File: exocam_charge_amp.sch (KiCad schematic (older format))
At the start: 17 parts, among them J1 jstsh6x1, U1 TLV2771CDBVT, U2 TLV2771CDBVT

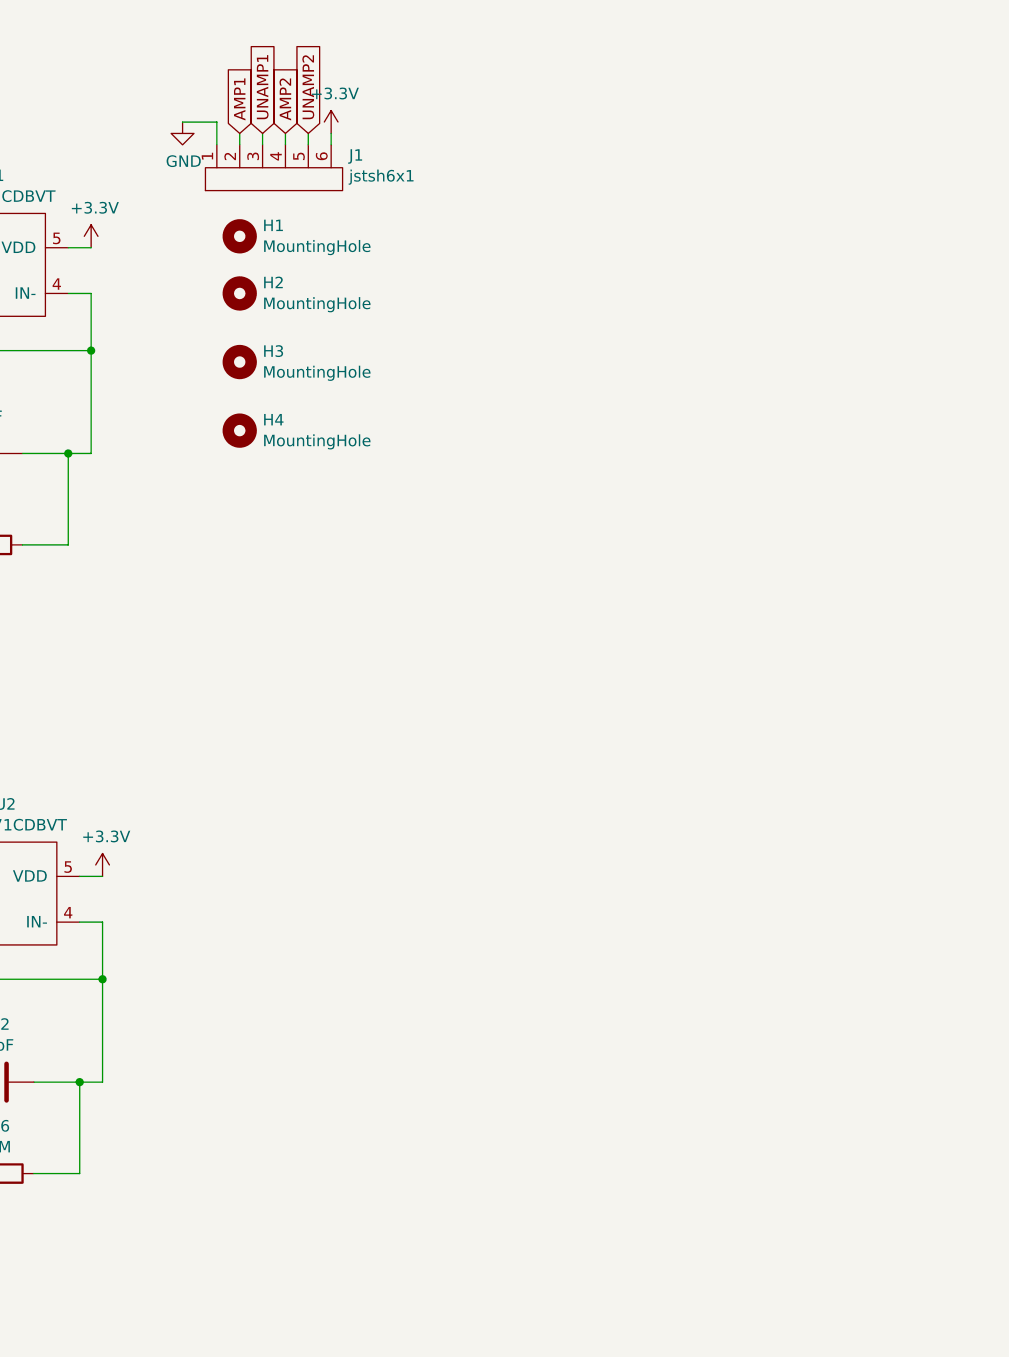
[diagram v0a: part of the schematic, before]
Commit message: updated shoulder to include the 3 amps
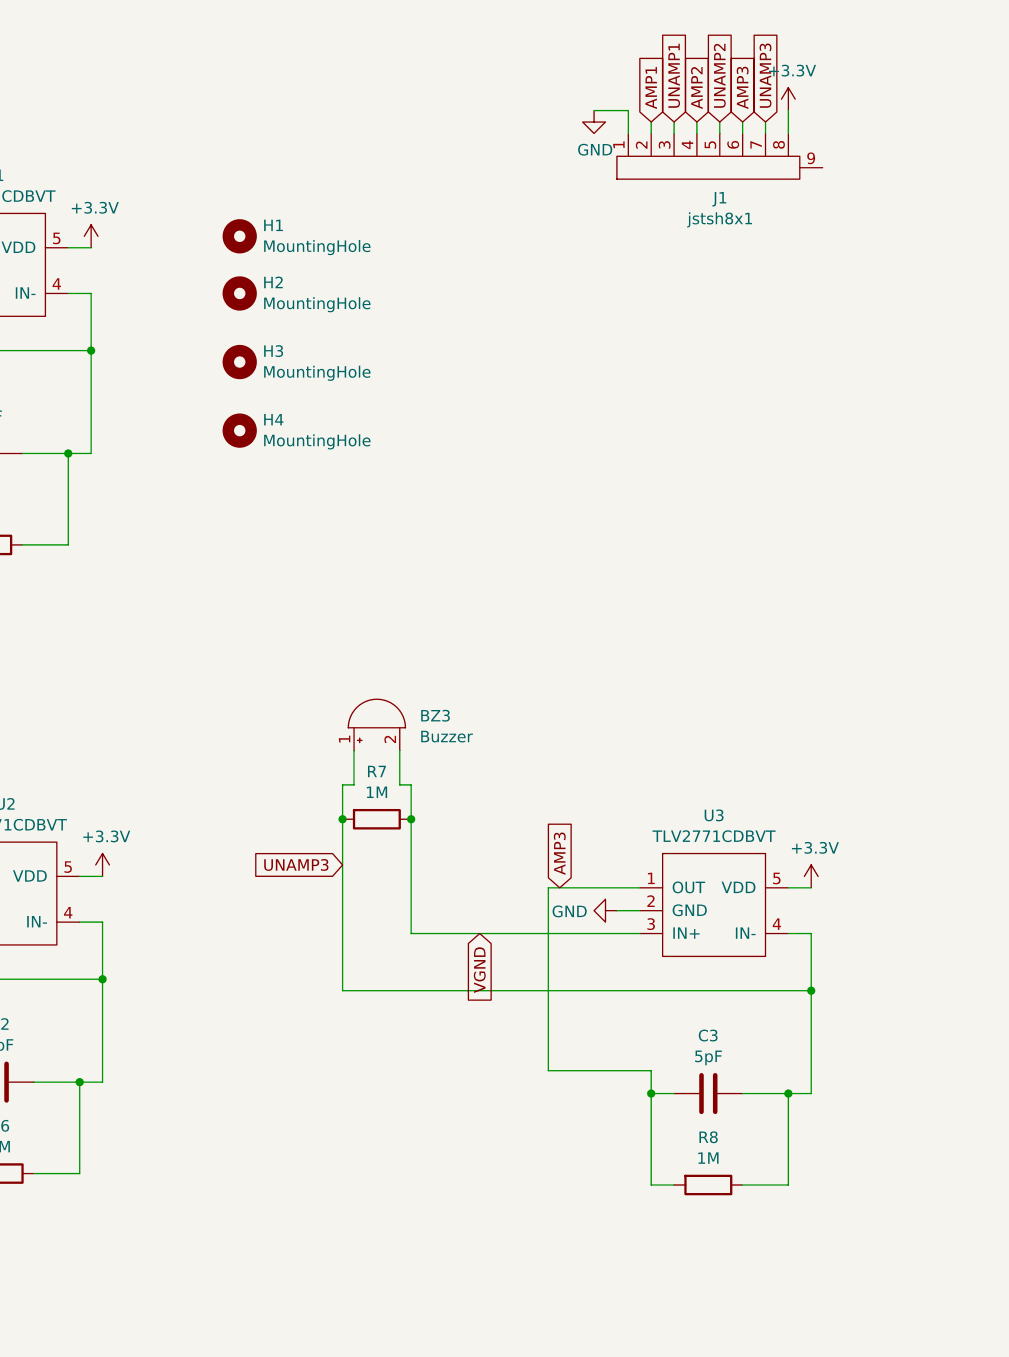
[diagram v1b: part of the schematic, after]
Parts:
- removed J1: jstsh6x1, exocam_charge_amp:jstsh6x1, symbol exocam_charge_amp:jstsh6x1
- added BZ3: Buzzer, exocam_charge_amp:jstsh2x1, symbol Device:Buzzer
- added C3: 5pF, exocam_charge_amp:0603_R, symbol Device:C
- added J1: jstsh8x1, exocam_charge_amp:jstsh8x1, symbol exocam_charge_amp:jstsh8x1
- added R7, R8: 1M, exocam_charge_amp:0603_R, symbol Device:R
- added U3: TLV2771CDBVT, exocam_charge_amp:TLV2271DBV, symbol exocam_charge_amp:TLV2771CDBVT
- BZ1: footprint exocam_charge_amp:piezo_buzzer -> exocam_charge_amp:piezo_buzzer_alt
- BZ2: footprint exocam_charge_amp:piezo_buzzer_alt -> exocam_charge_amp:jstsh2x1
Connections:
- net +3V3: now also J1.8, U3.5 (VDD)
- net AMP1: now also J1.2
- net AMP2: now also J1.4
- net GND: now also J1.1, U3.2 (GND)
- net UNAMP1: now also J1.3
- net UNAMP2: now also J1.5
- net VGND: now also BZ3.2 (+), R7.1, U3.3 (IN+)
- new net AMP3: C3.2, J1.6, R8.2, U3.1 (OUT)
- new net UNAMP3: BZ3.1 (-), C3.1, J1.7, R7.2, R8.1, U3.4 (IN-)
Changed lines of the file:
@@
 F 0 "BZ1" V 1901 613 50  0000 R CNN
 F 1 "Buzzer" V 1810 613 50  0000 R CNN
-F 2 "exocam_charge_amp:piezo_buzzer" V 1825 900 50  0001 C CNN
+F 2 "exocam_charge_amp:piezo_buzzer_alt" V 1825 900 50  0001 C CNN
 F 3 "~" V 1825 900 50  0001 C CNN
 	1    1850 800
@@
 F 0 "BZ2" V 1951 3363 50  0000 R CNN
 F 1 "Buzzer" V 1860 3363 50  0000 R CNN
-F 2 "exocam_charge_amp:piezo_buzzer_alt" V 1875 3650 50  0001 C CNN
+F 2 "exocam_charge_amp:jstsh2x1" V 1875 3650 50  0001 C CNN
 F 3 "~" V 1875 3650 50  0001 C CNN
 	1    1900 3550
@@
 Text GLabel 2350 4450 3    50   Input ~ 0
 VGND
-$Comp
-L exocam_charge_amp:jstsh6x1 J1
-U 1 1 60E1AF6A
-P 4250 1150
-F 0 "J1" V 4304 522 50  0000 R CNN
-F 1 "jstsh6x1" V 4213 522 50  0000 R CNN
-F 2 "exocam_charge_amp:jstsh6x1" H 4200 1300 50  0001 C CNN
-F 3 "" H 4200 1300 50  0001 C CNN
-	1    4250 1150
-	0    -1   -1   0
-$EndComp
-$Comp
-L power:+3.3V #PWR0104
-U 1 1 60E1C732
-P 4800 1000
-F 0 "#PWR0104" H 4800 850 50  0001 C CNN
-F 1 "+3.3V" H 4815 1173 50  0000 C CNN
-F 2 "" H 4800 1000 50  0001 C CNN
-F 3 "" H 4800 1000 50  0001 C CNN
-	1    4800 1000
-	1    0    0    -1
-$EndComp
-Wire Wire Line
-	4800 1050 4800 1000
-$Comp
-L power:GND #PWR0105
-U 1 1 60E1EDAD
-P 4150 950
-F 0 "#PWR0105" H 4150 700 50  0001 C CNN
-F 1 "GND" H 4155 777 50  0000 C CNN
-F 2 "" H 4150 950 50  0001 C CNN
-F 3 "" H 4150 950 50  0001 C CNN
-	1    4150 950
-	1    0    0    -1
-$EndComp
-Wire Wire Line
-	4300 1050 4300 950
-Wire Wire Line
-	4300 950  4150 950
-Text GLabel 4400 1000 1    50   Input ~ 0
-AMP1
-Wire Wire Line
-	4400 1050 4400 1000
-Text GLabel 4500 1000 1    50   Input ~ 0
-UNAMP1
-Wire Wire Line
-	4500 1000 4500 1050
-Text GLabel 4600 1000 1    50   Input ~ 0
-AMP2
-Wire Wire Line
-	4600 1000 4600 1050
-Text GLabel 4700 1000 1    50   Input ~ 0
-UNAMP2
-Wire Wire Line
-	4700 1000 4700 1050
 Wire Wire Line
 	1750 3950 1750 4700
@@
 Text GLabel 2700 1500 1    50   Input ~ 0
 AMP1
+$Comp
+L Device:C C3
+U 1 1 60E53BF7
+P 6450 5200
+F 0 "C3" V 6198 5200 50  0000 C CNN
+F 1 "5pF" V 6289 5200 50  0000 C CNN
+F 2 "exocam_charge_amp:0603_R" H 6488 5050 50  0001 C CNN
+F 3 "~" H 6450 5200 50  0001 C CNN
+	1    6450 5200
+	0    1    1    0
+$EndComp
+Wire Wire Line
+	6200 5200 6300 5200
+Wire Wire Line
+	6600 5200 6800 5200
+$Comp
+L Device:R R8
+U 1 1 60E53BFF
+P 6450 5600
+F 0 "R8" V 6243 5600 50  0000 C CNN
+F 1 "1M" V 6334 5600 50  0000 C CNN
+F 2 "exocam_charge_amp:0603_R" V 6380 5600 50  0001 C CNN
+F 3 "~" H 6450 5600 50  0001 C CNN
+	1    6450 5600
+	0    1    1    0
+$EndComp
+Wire Wire Line
+	6300 5600 6200 5600
+Wire Wire Line
+	6200 5600 6200 5200
+Wire Wire Line
+	6600 5600 6800 5600
+Wire Wire Line
+	6800 5600 6800 5200
+$Comp
+L Device:Buzzer BZ3
+U 1 1 60E53C09
+P 5000 3600
+F 0 "BZ3" V 5051 3413 50  0000 R CNN
+F 1 "Buzzer" V 4960 3413 50  0000 R CNN
+F 2 "exocam_charge_amp:jstsh2x1" V 4975 3700 50  0001 C CNN
+F 3 "~" V 4975 3700 50  0001 C CNN
+	1    5000 3600
+	0    -1   -1   0
+$EndComp
+$Comp
+L Device:R R7
+U 1 1 60E53C0F
+P 5000 4000
+F 0 "R7" V 4793 4000 50  0000 C CNN
+F 1 "1M" V 4884 4000 50  0000 C CNN
+F 2 "exocam_charge_amp:0603_R" V 4930 4000 50  0001 C CNN
+F 3 "~" H 5000 4000 50  0001 C CNN
+	1    5000 4000
+	0    1    1    0
+$EndComp
+Wire Wire Line
+	4850 4000 4850 3850
+Wire Wire Line
+	4850 3850 4900 3850
+Wire Wire Line
+	5150 4000 5150 3850
+Wire Wire Line
+	5150 3850 5100 3850
+Connection ~ 4850 4000
+$Comp
+L exocam_charge_amp:TLV2771CDBVT U3
+U 1 1 60E53C1A
+P 6450 4200
+F 0 "U3" H 6475 4415 50  0000 C CNN
+F 1 "TLV2771CDBVT" H 6475 4324 50  0000 C CNN
+F 2 "exocam_charge_amp:TLV2271DBV" H 6450 4200 50  0001 C CNN
+F 3 "" H 6450 4200 50  0001 C CNN
+	1    6450 4200
+	1    0    0    -1
+$EndComp
+$Comp
+L power:GND #PWR0104
+U 1 1 60E53C20
+P 6050 4400
+F 0 "#PWR0104" H 6050 4150 50  0001 C CNN
+F 1 "GND" V 6055 4272 50  0000 R CNN
+F 2 "" H 6050 4400 50  0001 C CNN
+F 3 "" H 6050 4400 50  0001 C CNN
+	1    6050 4400
+	0    1    1    0
+$EndComp
+Wire Wire Line
+	6050 4400 6150 4400
+Wire Wire Line
+	6150 4300 5750 4300
+Wire Wire Line
+	5750 4300 5750 5100
+Wire Wire Line
+	5750 5100 6200 5100
+Wire Wire Line
+	6200 5100 6200 5200
+Connection ~ 6200 5200
+Wire Wire Line
+	6800 4500 6900 4500
+Wire Wire Line
+	6900 4500 6900 4750
+Wire Wire Line
+	6900 5200 6800 5200
+Connection ~ 6800 5200
+Wire Wire Line
+	4850 4750 6900 4750
+Connection ~ 6900 4750
+Wire Wire Line
+	6900 4750 6900 5200
+Wire Wire Line
+	4900 3850 4900 3700
+Wire Wire Line
+	5100 3850 5100 3700
+Connection ~ 5150 4000
+Wire Wire Line
+	5150 4500 6150 4500
+Wire Wire Line
+	5150 4000 5150 4500
+Text GLabel 5450 4500 3    50   Input ~ 0
+VGND
+Wire Wire Line
+	4850 4000 4850 4750
+Text GLabel 4850 4200 0    50   Input ~ 0
+UNAMP3
+Text GLabel 5800 4300 1    50   Input ~ 0
+AMP3
+$Comp
+L power:+3.3V #PWR0105
+U 1 1 60E53C3C
+P 6900 4300
+F 0 "#PWR0105" H 6900 4150 50  0001 C CNN
+F 1 "+3.3V" H 6915 4473 50  0000 C CNN
+F 2 "" H 6900 4300 50  0001 C CNN
+F 3 "" H 6900 4300 50  0001 C CNN
+	1    6900 4300
+	1    0    0    -1
+$EndComp
+Wire Wire Line
+	6800 4300 6900 4300
+$Comp
+L exocam_charge_amp:jstsh8x1 J1
+U 1 1 60E61A1E
+P 6050 1100
+F 0 "J1" V 5867 647 50  0000 C CNN
+F 1 "jstsh8x1" V 5776 647 50  0000 C CNN
+F 2 "exocam_charge_amp:jstsh8x1" H 6000 1250 50  0001 C CNN
+F 3 "" H 6000 1250 50  0001 C CNN
+	1    6050 1100
+	0    -1   -1   0
+$EndComp
+$Comp
+L power:GND #PWR0109
+U 1 1 60E62B54
+P 5950 900
+F 0 "#PWR0109" H 5950 650 50  0001 C CNN
+F 1 "GND" H 5955 727 50  0000 C CNN
+F 2 "" H 5950 900 50  0001 C CNN
+F 3 "" H 5950 900 50  0001 C CNN
+	1    5950 900
+	1    0    0    -1
+$EndComp
+Wire Wire Line
+	6100 1000 6100 900
+Wire Wire Line
+	6100 900  5950 900
+Text GLabel 6200 950  1    50   Input ~ 0
+AMP1
+Text GLabel 6300 950  1    50   Input ~ 0
+UNAMP1
+Text GLabel 6400 950  1    50   Input ~ 0
+AMP2
+Text GLabel 6500 950  1    50   Input ~ 0
+UNAMP2
+Text GLabel 6600 950  1    50   Input ~ 0
+AMP3
+Text GLabel 6700 950  1    50   Input ~ 0
+UNAMP3
+$Comp
+L power:+3.3V #PWR0110
+U 1 1 60E67236
+P 6800 900
+F 0 "#PWR0110" H 6800 750 50  0001 C CNN
+F 1 "+3.3V" H 6815 1073 50  0000 C CNN
+F 2 "" H 6800 900 50  0001 C CNN
+F 3 "" H 6800 900 50  0001 C CNN
+	1    6800 900
+	1    0    0    -1
+$EndComp
+Wire Wire Line
+	6800 900  6800 1000
+Wire Wire Line
+	6200 950  6200 1000
+Wire Wire Line
+	6300 950  6300 1000
+Wire Wire Line
+	6400 950  6400 1000
+Wire Wire Line
+	6500 950  6500 1000
+Wire Wire Line
+	6600 950  6600 1000
+Wire Wire Line
+	6700 950  6700 1000
 $EndSCHEMATC
